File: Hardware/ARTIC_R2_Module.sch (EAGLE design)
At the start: 116 parts, among them J25 U.FL, K1 TLP3475R, Q2 5.8A/30V/35mΩ, U1 ADM4210-1, U2 1.8V/100mA, U3 ARTIC_R2, U4 RFPA0133, U5 AS179-92LF, U6 3.0V, X1 CRYSTAL-TCXO-26MHZ

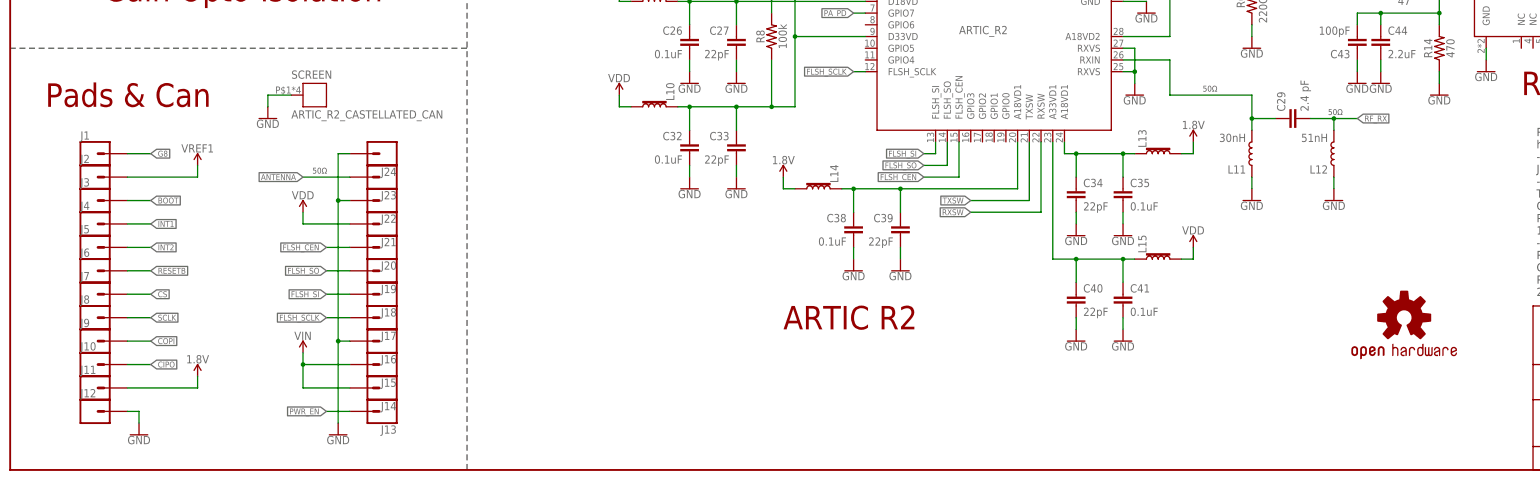
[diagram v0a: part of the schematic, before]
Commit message: Adding better castellated pads. Correcting cutouts for screen tabs.
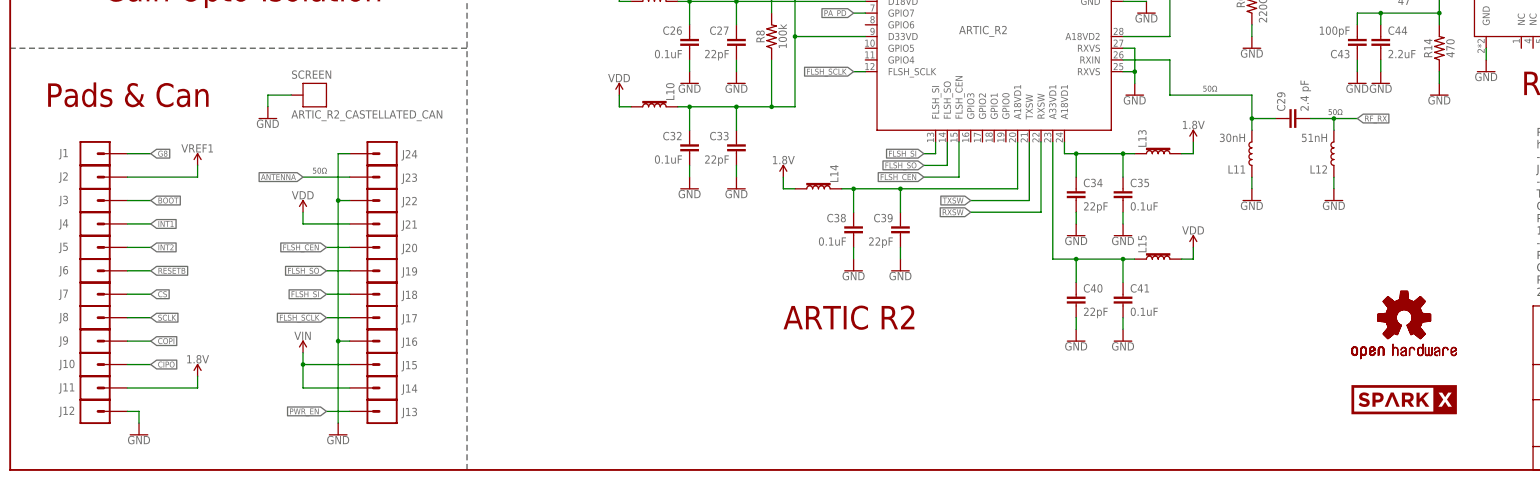
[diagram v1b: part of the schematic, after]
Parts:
- added LOGO3: OSHW-LOGOS, SparkFun-Aesthetics:OSHW-LOGOS
- added SPARKX2: SPARKX-LOGO4, SparkX:SPARKX-LOGO4
- J1, J10, J11, J12, J13, J14, J15, J16, J17, J18, J19, J2, J20, J21, J22, J23, J24, J3, J4, J5, J6, J7, J8, J9: value (none) -> CONN_01_CASTELLATED_4LAYER; device New_Parts_Connectors:CONN_01_CASTELLATEDCASTELLATED -> New_Parts_Connectors:CONN_01_CASTELLATED_4LAYER

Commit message: Updated the screening can
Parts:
- J1, J10, J11, J12, J13, J14, J15, J16, J17, J18, J19, J2, J20, J21, J22, J23, J24, J3, J4, J5, J6, J7, J8, J9: value CONN_01_CASTELLATED_4LAYER -> CONN_01_CASTELLATED_4LAYERWITHOUT_VIA; device New_Parts_Connectors:CONN_01_CASTELLATED_4LAYER -> New_Parts_Connectors:CONN_01_CASTELLATED_4LAYERWITHOUT_VIA
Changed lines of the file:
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@@
 <part name="SUPPLY2" library="SparkFun-PowerSymbols" deviceset="VDD" device=""/>
 <part name="SUPPLY3" library="SparkFun-PowerSymbols" deviceset="VDD" device=""/>
-<part name="J2" library="New_Parts_Connectors" deviceset="CONN_01_CASTELLATED_4LAYER" device="" value=""/>
+<part name="J2" library="New_Parts_Connectors" deviceset="CONN_01_CASTELLATED_4LAYER" device="WITHOUT_VIA" value=""/>
 <part name="GND34" library="SparkFun-PowerSymbols" deviceset="GND" device=""/>
-<part name="J3" library="New_Parts_Connectors" deviceset="CONN_01_CASTELLATED_4LAYER" device="" value=""/>
-<part name="J4" library="New_Parts_Connectors" deviceset="CONN_01_CASTELLATED_4LAYER" device="" value=""/>
-<part name="J1" library="New_Parts_Connectors" deviceset="CONN_01_CASTELLATED_4LAYER" device="" value=""/>
-<part name="J5" library="New_Parts_Connectors" deviceset="CONN_01_CASTELLATED_4LAYER" device="" value=""/>
-<part name="J6" library="New_Parts_Connectors" deviceset="CONN_01_CASTELLATED_4LAYER" device="" value=""/>
-<part name="J7" library="New_Parts_Connectors" deviceset="CONN_01_CASTELLATED_4LAYER" device="" value=""/>
-<part name="J8" library="New_Parts_Connectors" deviceset="CONN_01_CASTELLATED_4LAYER" device="" value=""/>
-<part name="J9" library="New_Parts_Connectors" deviceset="CONN_01_CASTELLATED_4LAYER" device="" value=""/>
-<part name="J10" library="New_Parts_Connectors" deviceset="CONN_01_CASTELLATED_4LAYER" device="" value=""/>
-<part name="J11" library="New_Parts_Connectors" deviceset="CONN_01_CASTELLATED_4LAYER" device="" value=""/>
-<part name="J12" library="New_Parts_Connectors" deviceset="CONN_01_CASTELLATED_4LAYER" device="" value=""/>
-<part name="J13" library="New_Parts_Connectors" deviceset="CONN_01_CASTELLATED_4LAYER" device="" value=""/>
-<part name="J14" library="New_Parts_Connectors" deviceset="CONN_01_CASTELLATED_4LAYER" device="" value=""/>
-<part name="J15" library="New_Parts_Connectors" deviceset="CONN_01_CASTELLATED_4LAYER" device="" value=""/>
-<part name="J16" library="New_Parts_Connectors" deviceset="CONN_01_CASTELLATED_4LAYER" device="" value=""/>
-<part name="J17" library="New_Parts_Connectors" deviceset="CONN_01_CASTELLATED_4LAYER" device="" value=""/>
-<part name="J18" library="New_Parts_Connectors" deviceset="CONN_01_CASTELLATED_4LAYER" device="" value=""/>
-<part name="J19" library="New_Parts_Connectors" deviceset="CONN_01_CASTELLATED_4LAYER" device="" value=""/>
-<part name="J20" library="New_Parts_Connectors" deviceset="CONN_01_CASTELLATED_4LAYER" device="" value=""/>
-<part name="J21" library="New_Parts_Connectors" deviceset="CONN_01_CASTELLATED_4LAYER" device="" value=""/>
-<part name="J22" library="New_Parts_Connectors" deviceset="CONN_01_CASTELLATED_4LAYER" device="" value=""/>
-<part name="J23" library="New_Parts_Connectors" deviceset="CONN_01_CASTELLATED_4LAYER" device="" value=""/>
-<part name="J24" library="New_Parts_Connectors" deviceset="CONN_01_CASTELLATED_4LAYER" device="" value=""/>
+<part name="J3" library="New_Parts_Connectors" deviceset="CONN_01_CASTELLATED_4LAYER" device="WITHOUT_VIA" value=""/>
+<part name="J4" library="New_Parts_Connectors" deviceset="CONN_01_CASTELLATED_4LAYER" device="WITHOUT_VIA" value=""/>
+<part name="J1" library="New_Parts_Connectors" deviceset="CONN_01_CASTELLATED_4LAYER" device="WITHOUT_VIA" value=""/>
+<part name="J5" library="New_Parts_Connectors" deviceset="CONN_01_CASTELLATED_4LAYER" device="WITHOUT_VIA" value=""/>
+<part name="J6" library="New_Parts_Connectors" deviceset="CONN_01_CASTELLATED_4LAYER" device="WITHOUT_VIA" value=""/>
+<part name="J7" library="New_Parts_Connectors" deviceset="CONN_01_CASTELLATED_4LAYER" device="WITHOUT_VIA" value=""/>
+<part name="J8" library="New_Parts_Connectors" deviceset="CONN_01_CASTELLATED_4LAYER" device="WITHOUT_VIA" value=""/>
+<part name="J9" library="New_Parts_Connectors" deviceset="CONN_01_CASTELLATED_4LAYER" device="WITHOUT_VIA" value=""/>
+<part name="J10" library="New_Parts_Connectors" deviceset="CONN_01_CASTELLATED_4LAYER" device="WITHOUT_VIA" value=""/>
+<part name="J11" library="New_Parts_Connectors" deviceset="CONN_01_CASTELLATED_4LAYER" device="WITHOUT_VIA" value=""/>
+<part name="J12" library="New_Parts_Connectors" deviceset="CONN_01_CASTELLATED_4LAYER" device="WITHOUT_VIA" value=""/>
+<part name="J13" library="New_Parts_Connectors" deviceset="CONN_01_CASTELLATED_4LAYER" device="WITHOUT_VIA" value=""/>
+<part name="J14" library="New_Parts_Connectors" deviceset="CONN_01_CASTELLATED_4LAYER" device="WITHOUT_VIA" value=""/>
+<part name="J15" library="New_Parts_Connectors" deviceset="CONN_01_CASTELLATED_4LAYER" device="WITHOUT_VIA" value=""/>
+<part name="J16" library="New_Parts_Connectors" deviceset="CONN_01_CASTELLATED_4LAYER" device="WITHOUT_VIA" value=""/>
+<part name="J17" library="New_Parts_Connectors" deviceset="CONN_01_CASTELLATED_4LAYER" device="WITHOUT_VIA" value=""/>
+<part name="J18" library="New_Parts_Connectors" deviceset="CONN_01_CASTELLATED_4LAYER" device="WITHOUT_VIA" value=""/>
+<part name="J19" library="New_Parts_Connectors" deviceset="CONN_01_CASTELLATED_4LAYER" device="WITHOUT_VIA" value=""/>
+<part name="J20" library="New_Parts_Connectors" deviceset="CONN_01_CASTELLATED_4LAYER" device="WITHOUT_VIA" value=""/>
+<part name="J21" library="New_Parts_Connectors" deviceset="CONN_01_CASTELLATED_4LAYER" device="WITHOUT_VIA" value=""/>
+<part name="J22" library="New_Parts_Connectors" deviceset="CONN_01_CASTELLATED_4LAYER" device="WITHOUT_VIA" value=""/>
+<part name="J23" library="New_Parts_Connectors" deviceset="CONN_01_CASTELLATED_4LAYER" device="WITHOUT_VIA" value=""/>
+<part name="J24" library="New_Parts_Connectors" deviceset="CONN_01_CASTELLATED_4LAYER" device="WITHOUT_VIA" value=""/>
 <part name="SUPPLY4" library="SparkFun-PowerSymbols" deviceset="VDD" device=""/>
 <part name="SUPPLY14" library="SparkFun-PowerSymbols" deviceset="VIN" device=""/>

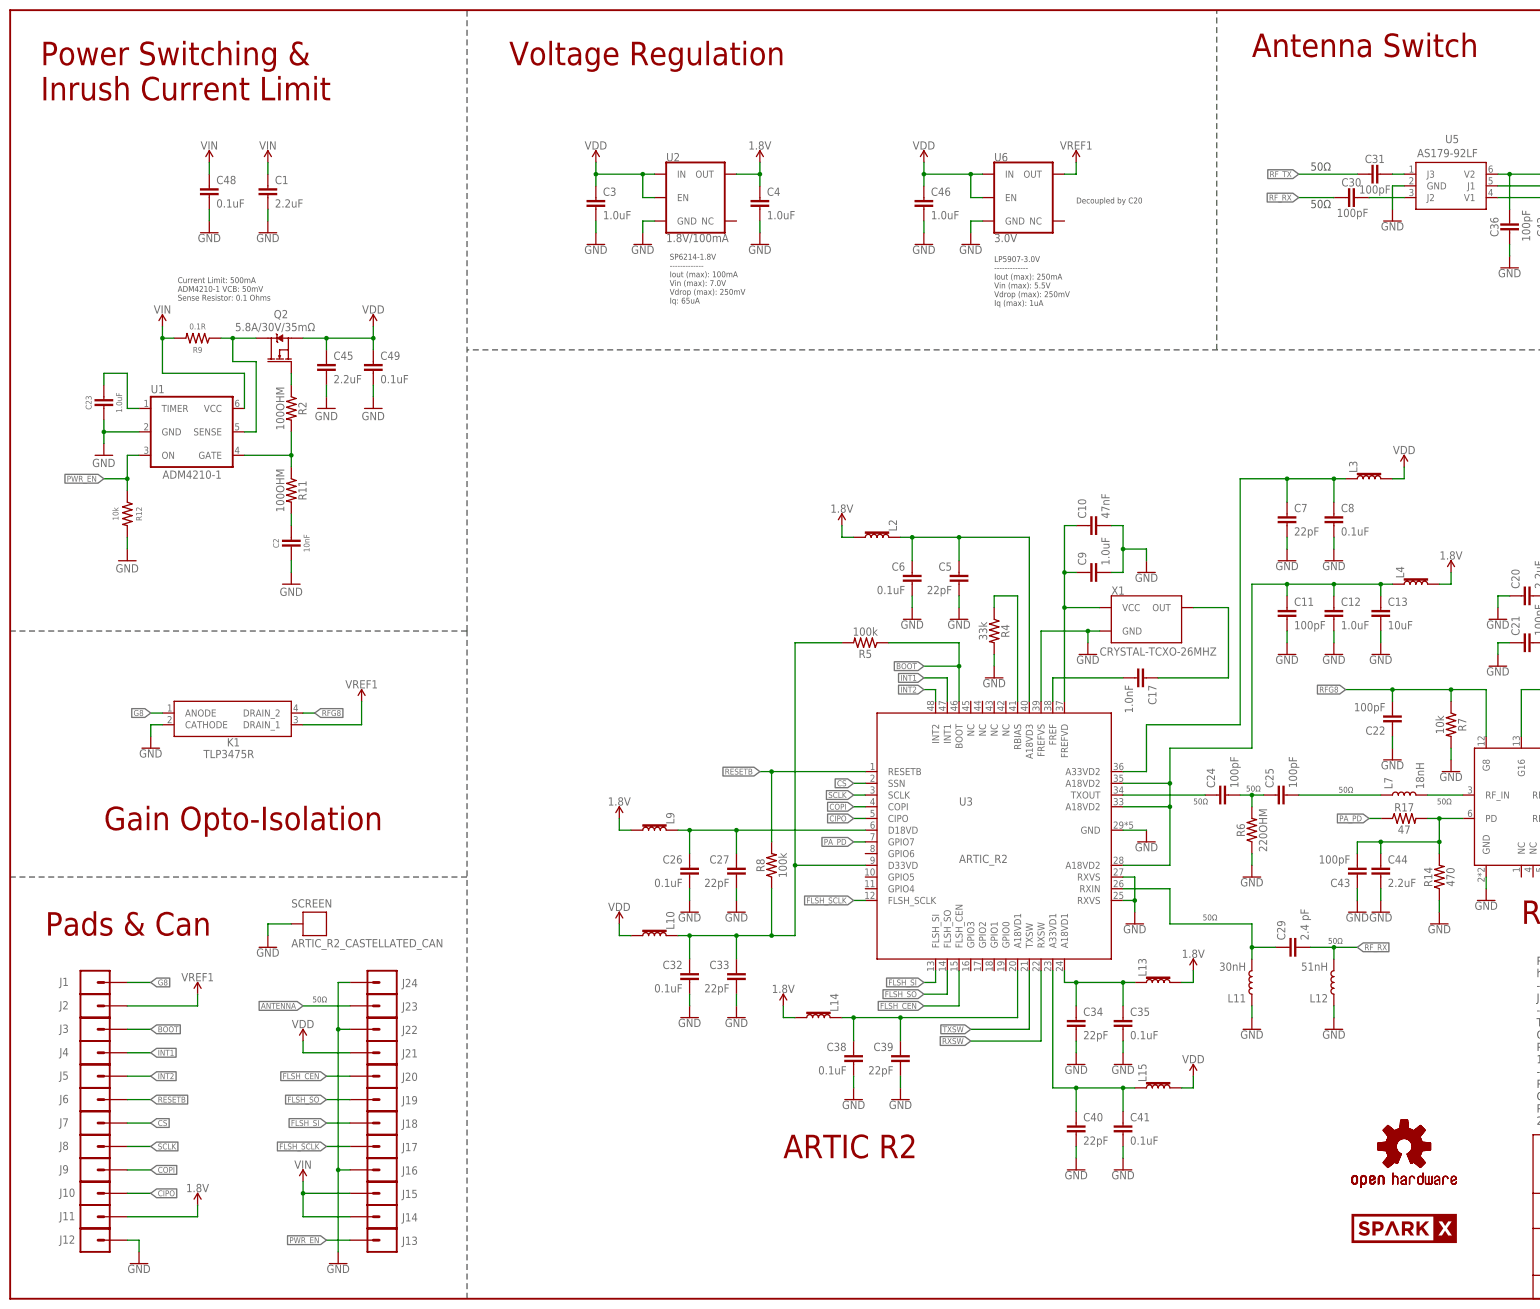
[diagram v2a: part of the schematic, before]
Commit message: Added the flash memory in USON format
The flash has its own power pin so it can be programmed independantly - without needing the ARTIC to be powered up and held in reset. The user will need to jump the flash power pad across to the adjacent VDD pad on their board.
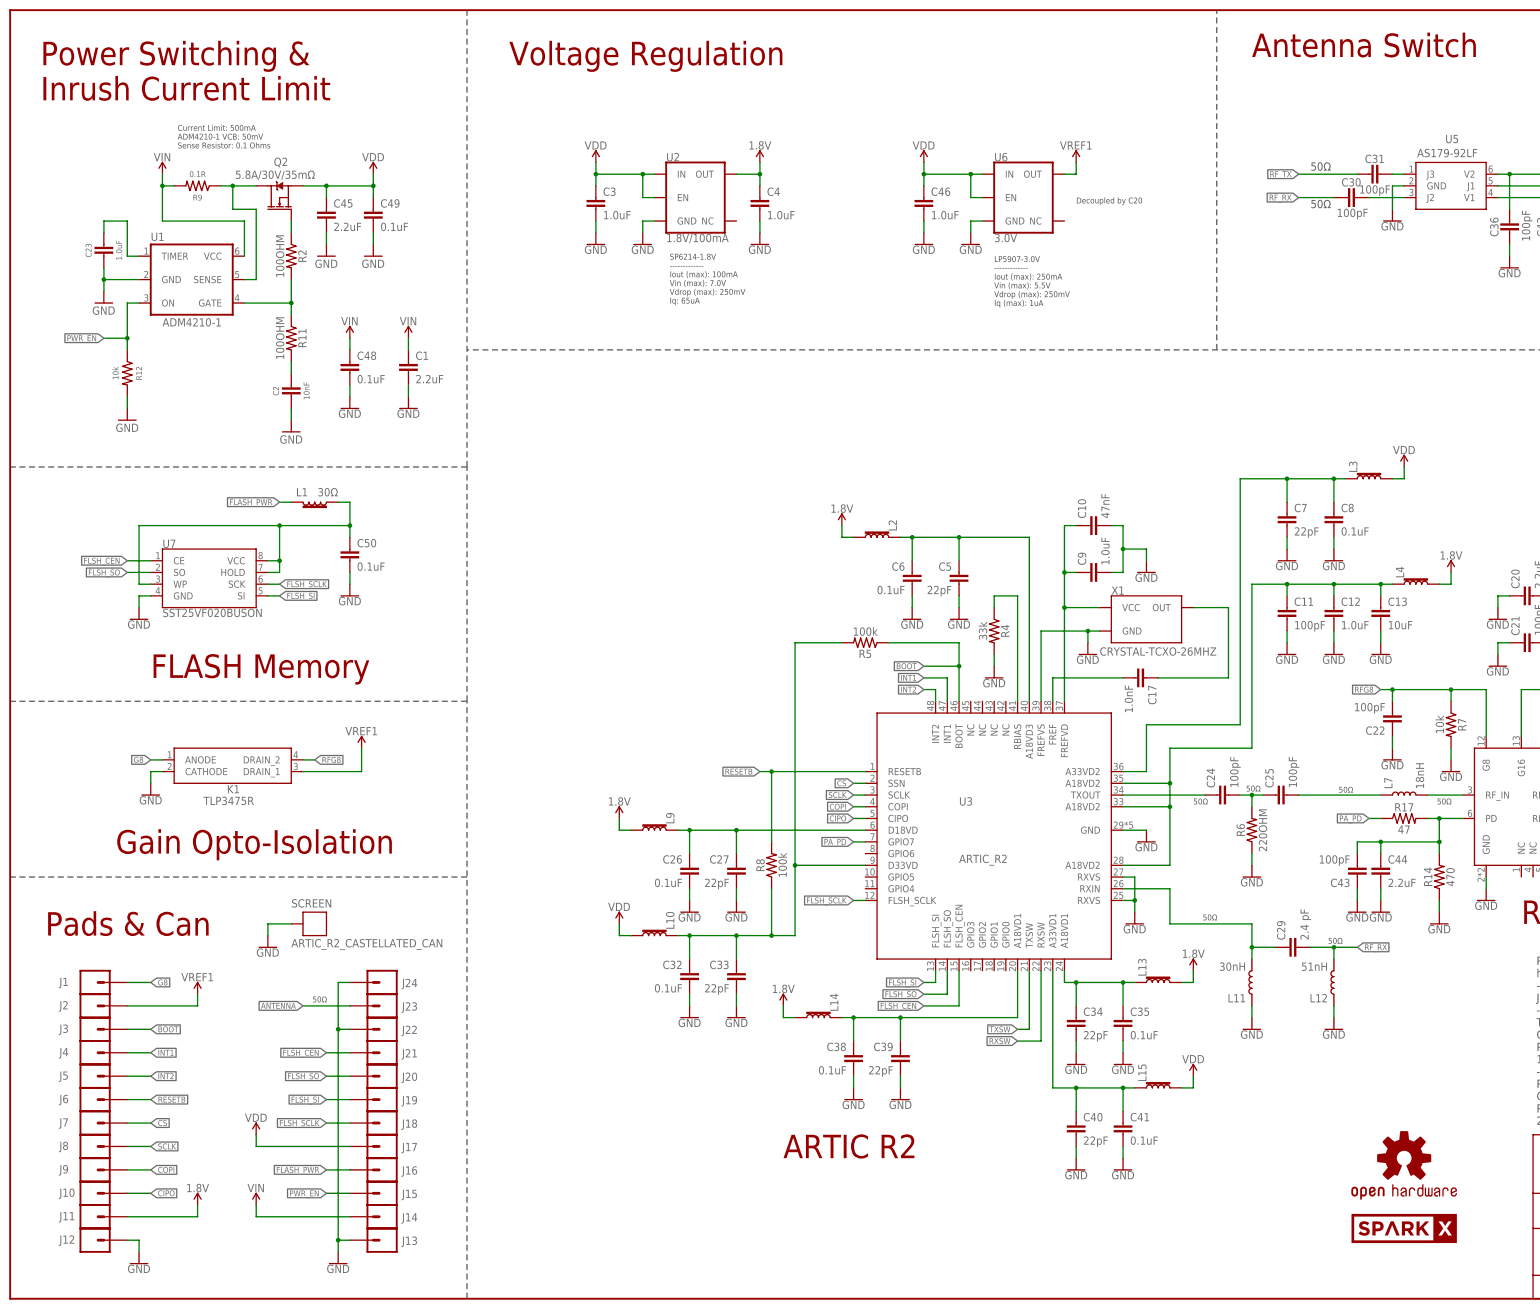
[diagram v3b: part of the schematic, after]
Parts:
- removed LOGO2: OSHW-LOGOS, SparkFun-Aesthetics:OSHW-LOGOS
- added C50: 0.1uF, SparkFun-Capacitors:0.1UF-0402T-6.3V-10%-X7R
- added L1: 30Ω, SparkFun-Coils:FERRITE_BEAD-0402-30OHM-100MHZ
- added U7: SST25VF020BUSON, New_Parts_IC-Memory:SST25VF020BUSON
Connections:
- new net FLASH_PWR: J16.1, L1.2
- new net FLASH_VCC: C50.1, L1.1, U7.HOLD, U7.VCC, U7.WP
- net FLSH_CEN: now also J21.1, U7.CE; no longer J20.1
- net FLSH_SCLK: now also J18.1, U7.SCK; no longer J17.1
- net FLSH_SI: now also J19.1, U7.SI; no longer J18.1
- net FLSH_SO: now also J20.1, U7.SO; no longer J19.1
- net GND: now also C50.2, J13.1, U7.GND; no longer J16.1
- net PWR_EN: now also J15.1; no longer J13.1
- net VDD: now also J17.1; no longer J21.1
- net VIN: no longer J15.1
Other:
- note added: "FLASH Memory"
- moved on the sheet: C1, C2, C23, C45, C48, C49, K1, Q2, R11, R12, R2, R9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
